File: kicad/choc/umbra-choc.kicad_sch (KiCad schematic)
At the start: 34 parts, among them SW1 SW_Push, SW10 SW_Push, SW11 SW_Push, SW12 SW_Push, SW13 SW_Push, SW14 SW_Push, SW15 SW_Push, SW16 SW_Push, SW17 SW_Push, SW18 SW_Push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

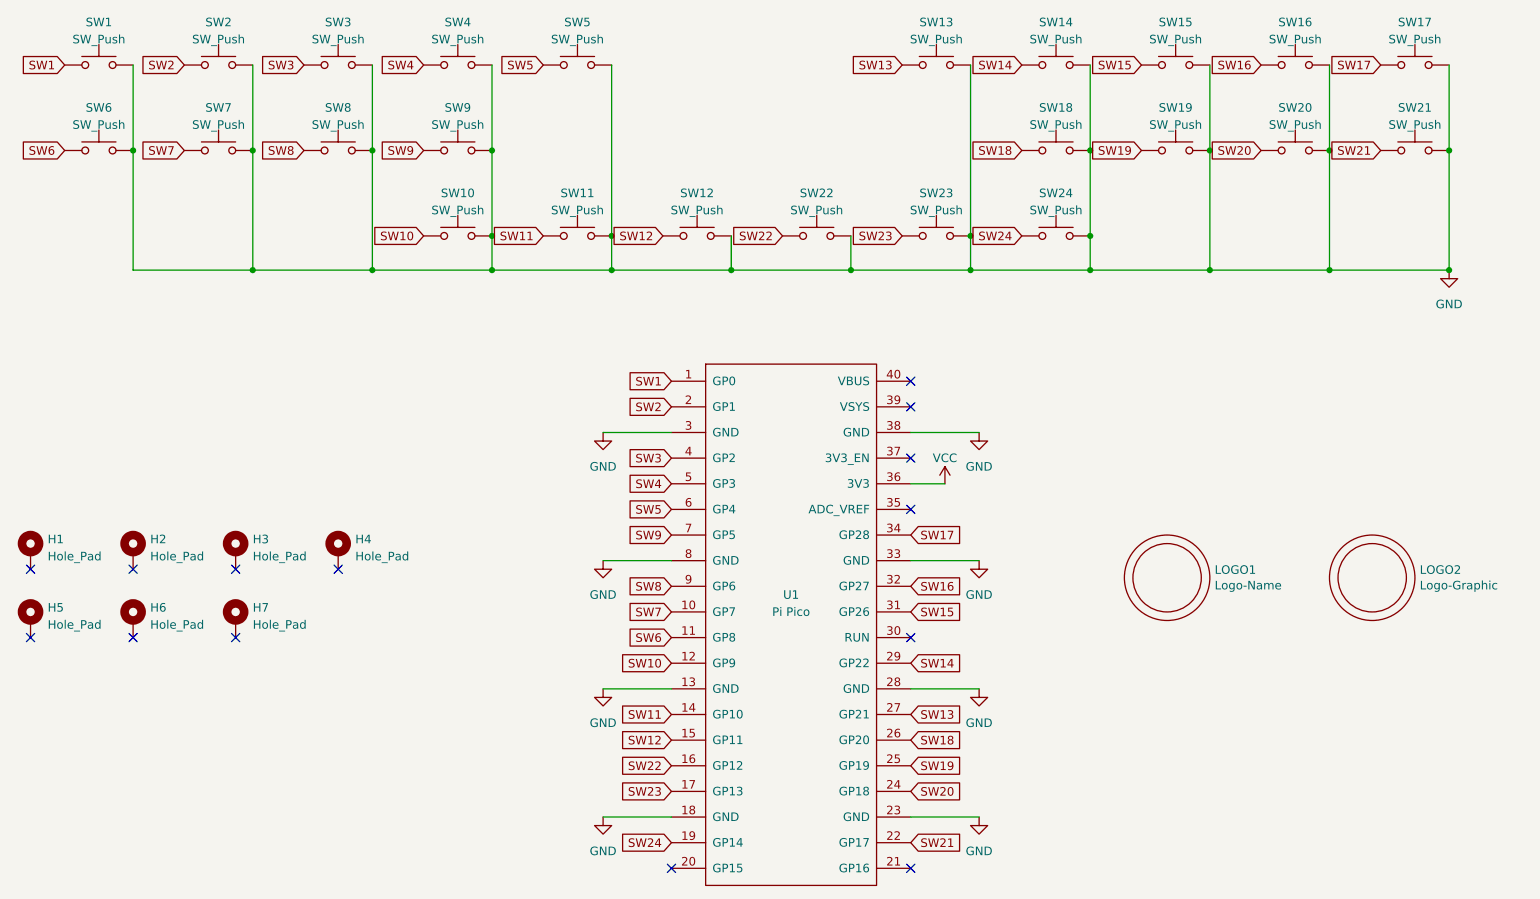
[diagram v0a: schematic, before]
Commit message: Update schematic global labels for GPIO assignment readability
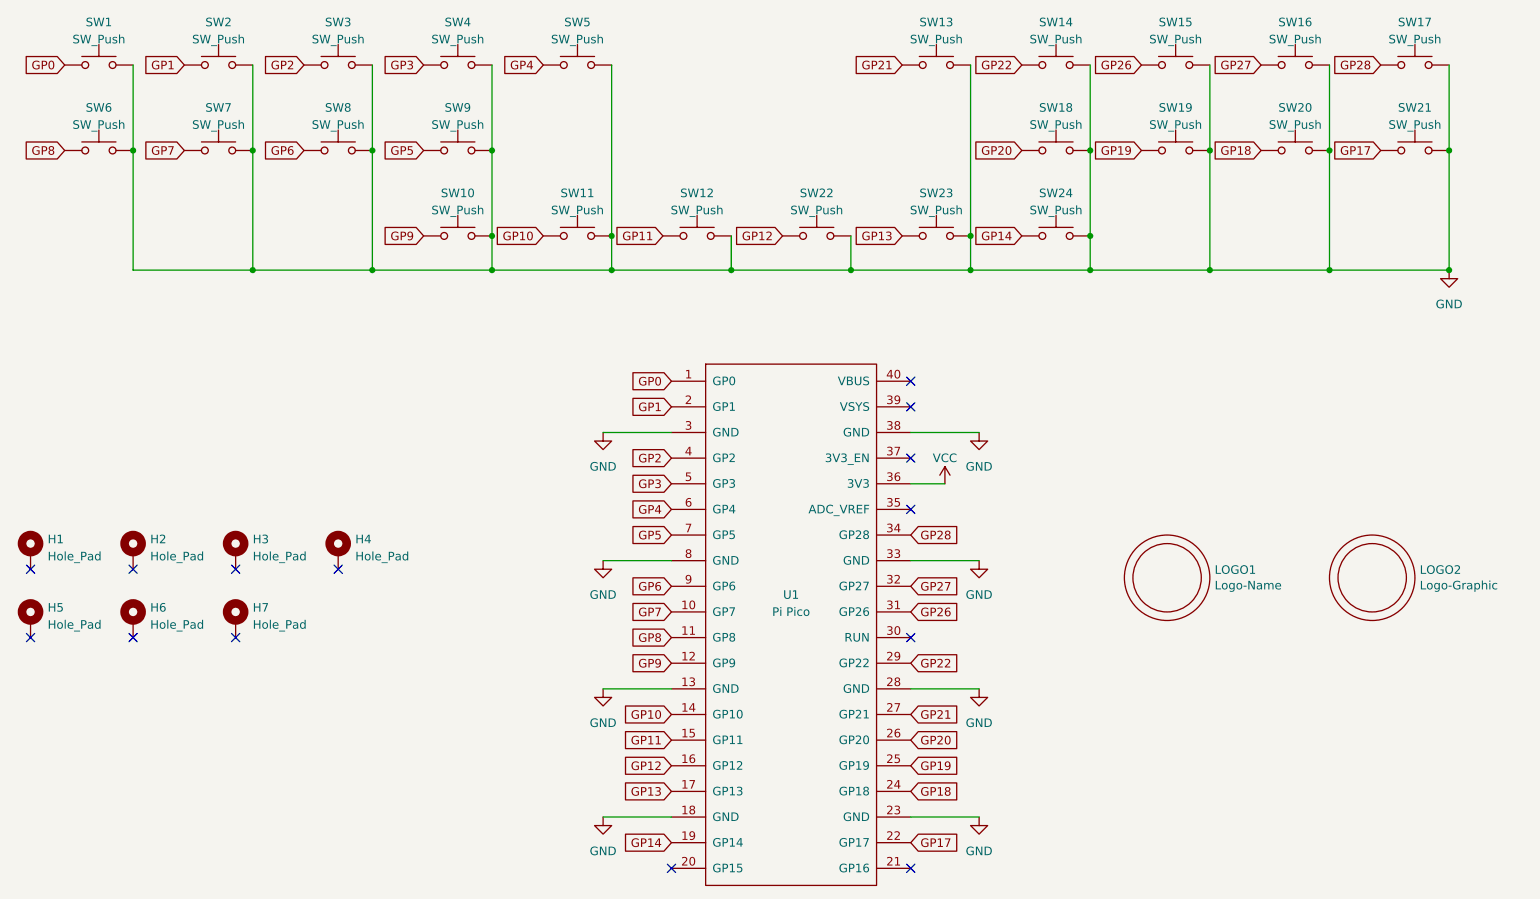
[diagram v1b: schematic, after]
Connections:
- net SW1 renamed GP0
- net SW10 renamed GP9
- net SW11 renamed GP10
- net SW12 renamed GP11
- net SW13 renamed GP21
- net SW14 renamed GP22
- net SW15 renamed GP26
- net SW16 renamed GP27
- net SW17 renamed GP28
- net SW18 renamed GP20
- net SW19 renamed GP19
- net SW2 renamed GP1
- net SW20 renamed GP18
- net SW21 renamed GP17
- net SW22 renamed GP12
- net SW23 renamed GP13
- net SW24 renamed GP14
- net SW3 renamed GP2
- net SW4 renamed GP3
- net SW5 renamed GP4
- net SW6 renamed GP8
- net SW7 renamed GP7
- net SW8 renamed GP6
- net SW9 renamed GP5
